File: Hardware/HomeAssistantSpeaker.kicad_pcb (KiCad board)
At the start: 2 copper layers, 53.3 x 50 mm, 31 parts, among them J1 USB_C_Receptacle_USB2.0, J2 Speaker, J3 Prog, J4 LED, U1 ESP32-WROOM-32, U2 LM1117-3.3, U3 MAX98357AETE+

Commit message: Silkscreen cleanup
* Moved overlaping silkscreen values
* Added gain setting info on the PCB
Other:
- net class Default removed
- board text added: "At most one populated R4 R5"
- board text added: "Output gain R4 100k 3dB R4 0R 6dB R4/R5 NC 9dB R5 0R 12dB R5 100k 15db"

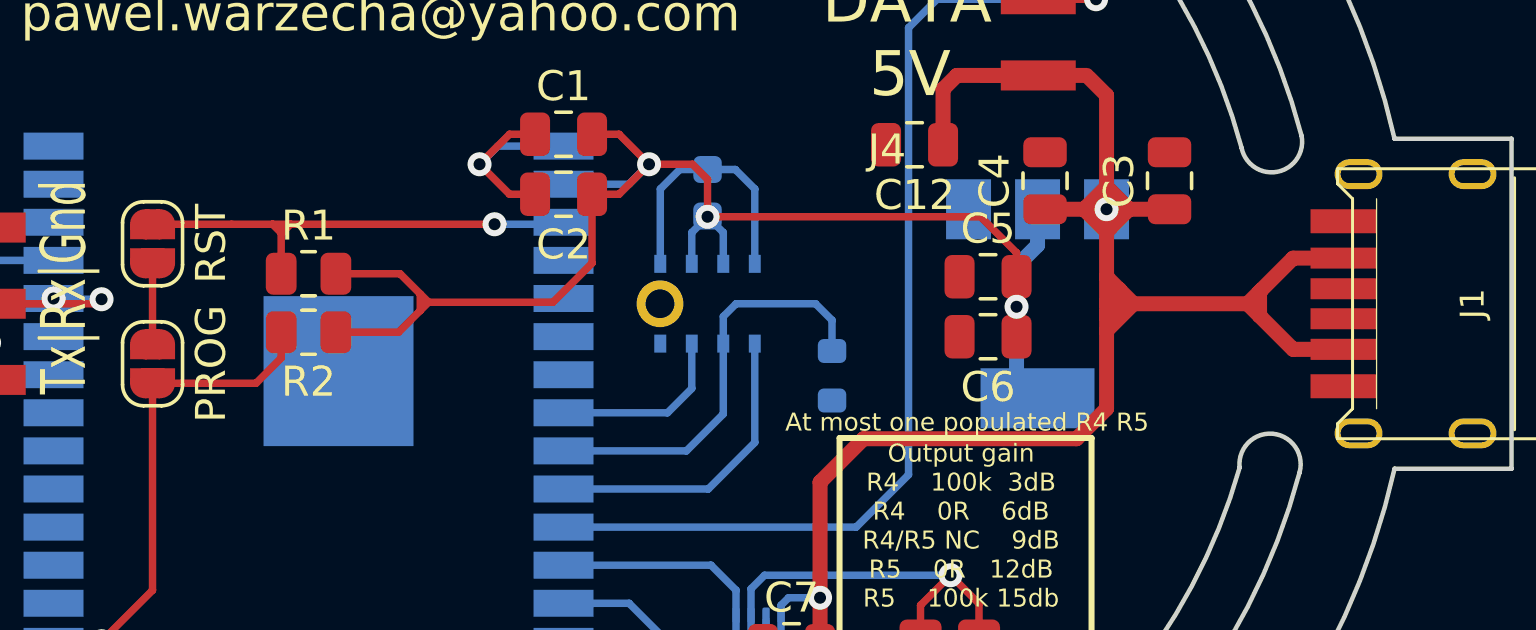
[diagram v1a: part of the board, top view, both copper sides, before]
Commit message: Rev B:
* Added missing resitiors for usb c power
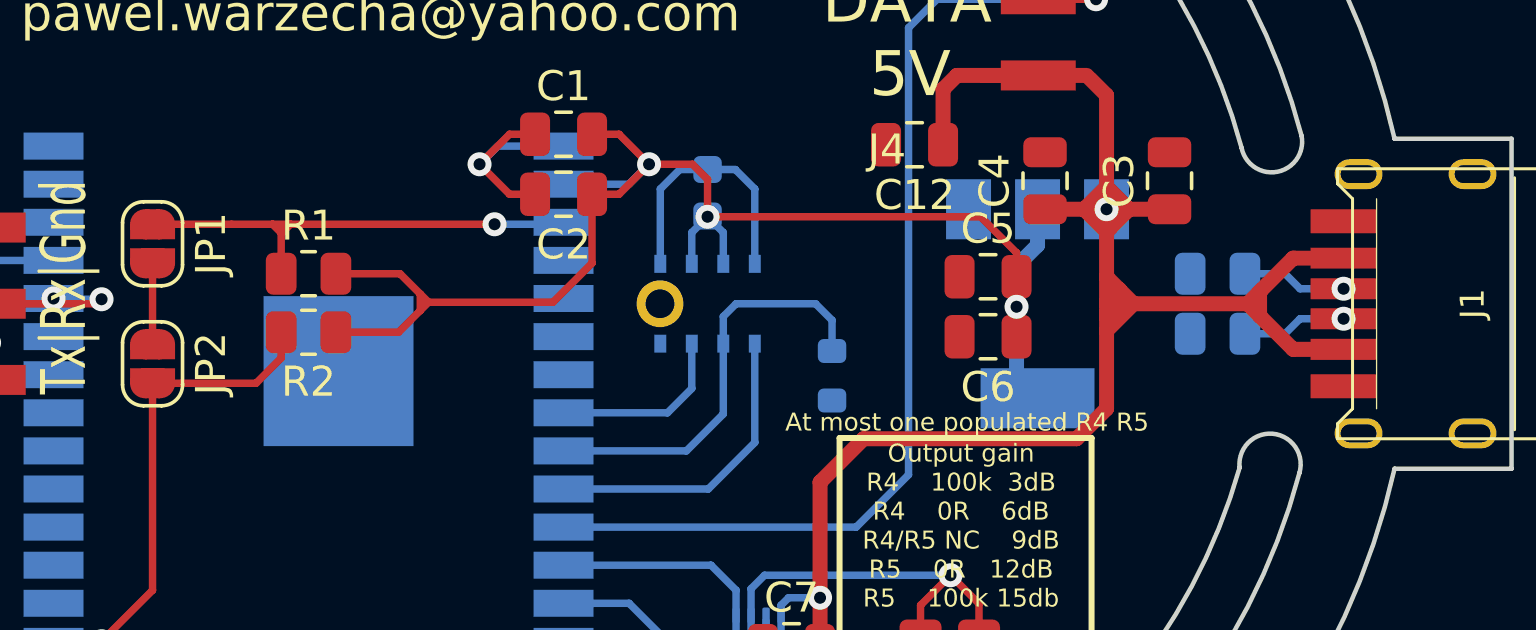
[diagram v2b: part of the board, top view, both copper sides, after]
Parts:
- added R6: 5k1, Resistor_SMD:R_0805_2012Metric, B.Cu at (118.5, 99.0)
- added R7: 5k1, Resistor_SMD:R_0805_2012Metric, B.Cu at (118.5, 101.0)
- FB1, FB2: value Ferrite_Bead_Small -> 20uH
- renumbered RST to JP1, PROG to JP2
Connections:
- U1 pad 16: Net-(U1-Pad16) -> unconnected-(U1-Pad16)
- U1 pad 17: Net-(U1-Pad17) -> unconnected-(U1-Pad17)
- U1 pad 18: Net-(U1-Pad18) -> unconnected-(U1-Pad18)
- U1 pad 19: Net-(U1-Pad19) -> unconnected-(U1-Pad19)
- U1 pad 20: Net-(U1-Pad20) -> unconnected-(U1-Pad20)
- U1 pad 21: Net-(U1-Pad21) -> unconnected-(U1-Pad21)
- U1 pad 22: Net-(U1-Pad22) -> unconnected-(U1-Pad22)
- U1 pad 23: Net-(U1-Pad23) -> unconnected-(U1-Pad23)
- U1 pad 24: Net-(U1-Pad24) -> unconnected-(U1-Pad24)
- U1 pad 26: Net-(U1-Pad26) -> unconnected-(U1-Pad26)
- U1 pad 27: Net-(U1-Pad27) -> unconnected-(U1-Pad27)
- U1 pad 28: Net-(U1-Pad28) -> unconnected-(U1-Pad28)
- U1 pad 29: Net-(U1-Pad29) -> unconnected-(U1-Pad29)
- U1 pad 30: Net-(U1-Pad30) -> unconnected-(U1-Pad30)
- U1 pad 31: Net-(U1-Pad31) -> unconnected-(U1-Pad31)
- U1 pad 32: Net-(U1-Pad32) -> unconnected-(U1-Pad32)
- U1 pad 33: Net-(U1-Pad33) -> unconnected-(U1-Pad33)
- U1 pad 36: Net-(U1-Pad36) -> unconnected-(U1-Pad36)
- U1 pad 37: Net-(U1-Pad37) -> unconnected-(U1-Pad37)
- U1 pad 4: Net-(U1-Pad4) -> unconnected-(U1-Pad4)
- U1 pad 5: Net-(U1-Pad5) -> unconnected-(U1-Pad5)
- U1 pad 6: Net-(U1-Pad6) -> unconnected-(U1-Pad6)
- U1 pad 7: Net-(U1-Pad7) -> unconnected-(U1-Pad7)
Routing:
- net Net-(J1-PadB5): track 0.00 -> 3.49 mm, vias 0 -> 1
- net Net-(J1-PadA5): track 0.00 -> 3.49 mm, vias 0 -> 1
